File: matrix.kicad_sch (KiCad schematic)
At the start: 130 parts, among them SW1 `, SW10 9, SW11 0, SW12 -, SW13 =, SW14 BKSPC, SW15 DEL, SW16 TAB, SW17 Q, SW18 W, SW19 E, SW2 1, SW20 R, SW21 T, SW22 Y, SW23 U, SW24 I, SW25 O, SW26 P, SW27 [{, SW28 ]}, SW29 \|, SW3 2, SW30 HOME, SW31 CAPS, SW32 A, SW33 S, SW34 D, SW35 F, SW36 G, SW37 H, SW38 J, SW39 K, SW4 3, SW40 L, SW41 ;:, SW42 '", SW43 ENTER, SW44 LSHIFT, SW45 Z, SW46 X, SW47 C, SW48 V, SW49 B, SW5 4, SW50 N, SW51 M, SW52 ,<, SW53 .>, SW54 /?, SW55 RSHIFT, SW56 UP, SW57 LCTRL, SW58 LWIN, SW59 LALT, SW6 5, SW60 SPACE, SW61 RALT, SW62 FN, SW63 LEFT, SW64 DOWN, SW65 RIGHT, SW7 6, SW8 7, SW9 8

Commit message: Wiring
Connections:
- net col10: no longer SW61.1
- net col5: now also SW60.1
- net col6: no longer SW60.1
- net col9: now also SW61.1
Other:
- moved on the sheet: D60, D61, SW60, SW61
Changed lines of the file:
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@@
   (junction (at 104.14 110.49) (diameter 0) (color 0 0 0 0)
   )
+  (junction (at 165.1 133.35) (diameter 0) (color 0 0 0 0)
+  )
   (junction (at 43.18 41.91) (diameter 0) (color 0 0 0 0)
   )
@@
   (junction (at 53.34 57.15) (diameter 0) (color 0 0 0 0)
   )
+  (junction (at 175.26 102.87) (diameter 0) (color 0 0 0 0)
+  )
   (junction (at 88.9 87.63) (diameter 0) (color 0 0 0 0)
   )
-  (junction (at 180.34 133.35) (diameter 0) (color 0 0 0 0)
-  )
   (junction (at 180.34 87.63) (diameter 0) (color 0 0 0 0)
   )
@@
   (junction (at 43.18 87.63) (diameter 0) (color 0 0 0 0)
   )
+  (junction (at 114.3 102.87) (diameter 0) (color 0 0 0 0)
+  )
   (junction (at 38.1 102.87) (diameter 0) (color 0 0 0 0)
   )
@@
   (junction (at 53.34 80.01) (diameter 0) (color 0 0 0 0)
   )
-  (junction (at 190.5 102.87) (diameter 0) (color 0 0 0 0)
-  )
   (junction (at 180.34 41.91) (diameter 0) (color 0 0 0 0)
   )
@@
   (junction (at 210.82 41.91) (diameter 0) (color 0 0 0 0)
   )
+  (junction (at 104.14 133.35) (diameter 0) (color 0 0 0 0)
+  )
   (junction (at 205.74 80.01) (diameter 0) (color 0 0 0 0)
   )
@@
   (junction (at 236.22 102.87) (diameter 0) (color 0 0 0 0)
   )
-  (junction (at 119.38 133.35) (diameter 0) (color 0 0 0 0)
-  )
   (junction (at 83.82 57.15) (diameter 0) (color 0 0 0 0)
   )
@@
   (junction (at 195.58 41.91) (diameter 0) (color 0 0 0 0)
   )
-  (junction (at 129.54 102.87) (diameter 0) (color 0 0 0 0)
-  )
   (junction (at 119.38 41.91) (diameter 0) (color 0 0 0 0)
   )
@@
     (stroke (width 0) (type default) (color 0 0 0 0))
   )
+  (wire (pts (xy 165.1 133.35) (xy 195.58 133.35))
+    (stroke (width 0) (type default) (color 0 0 0 0))
+  )
   (wire (pts (xy 149.86 64.77) (xy 165.1 64.77))
     (stroke (width 0) (type default) (color 0 0 0 0))
@@
     (stroke (width 0) (type default) (color 0 0 0 0))
   )
-  (wire (pts (xy 58.42 133.35) (xy 119.38 133.35))
-    (stroke (width 0) (type default) (color 0 0 0 0))
-  )
   (wire (pts (xy 180.34 87.63) (xy 195.58 87.63))
     (stroke (width 0) (type default) (color 0 0 0 0))
@@
     (stroke (width 0) (type default) (color 0 0 0 0))
   )
-  (wire (pts (xy 190.5 102.87) (xy 190.5 125.73))
+  (wire (pts (xy 175.26 102.87) (xy 175.26 125.73))
     (stroke (width 0) (type default) (color 0 0 0 0))
   )
@@
     (stroke (width 0) (type default) (color 0 0 0 0))
   )
-  (wire (pts (xy 180.34 133.35) (xy 195.58 133.35))
-    (stroke (width 0) (type default) (color 0 0 0 0))
-  )
   (wire (pts (xy 88.9 87.63) (xy 104.14 87.63))
     (stroke (width 0) (type default) (color 0 0 0 0))
@@
     (stroke (width 0) (type default) (color 0 0 0 0))
   )
-  (wire (pts (xy 129.54 102.87) (xy 129.54 125.73))
+  (wire (pts (xy 114.3 102.87) (xy 114.3 125.73))
     (stroke (width 0) (type default) (color 0 0 0 0))
   )
@@
     (stroke (width 0) (type default) (color 0 0 0 0))
   )
+  (wire (pts (xy 104.14 133.35) (xy 165.1 133.35))
+    (stroke (width 0) (type default) (color 0 0 0 0))
+  )
   (wire (pts (xy 104.14 87.63) (xy 119.38 87.63))
     (stroke (width 0) (type default) (color 0 0 0 0))
@@
     (stroke (width 0) (type default) (color 0 0 0 0))
   )
-  (wire (pts (xy 119.38 133.35) (xy 180.34 133.35))
+  (wire (pts (xy 58.42 133.35) (xy 104.14 133.35))
     (stroke (width 0) (type default) (color 0 0 0 0))
   )
@@
     (pin "2")
   )
-  (symbol (lib_id "Device:D") (at 180.34 129.54 90) (unit 1)
-    (in_bom yes) (on_board yes) (fields_autoplaced)
-    (property "Reference" "D61" (id 0) (at 182.88 128.2699 90)
-      (effects (font (size 1.27 1.27)) (justify right))
-    )
-    (property "Value" "D" (id 1) (at 182.88 130.8099 90)
-      (effects (font (size 1.27 1.27)) (justify right))
-    )
-    (property "Footprint" "Diode_SMD:D_SOD-123" (id 2) (at 180.34 129.54 0)
-      (effects (font (size 1.27 1.27)) hide)
-    )
-    (property "Datasheet" "~" (id 3) (at 180.34 129.54 0)
+  (symbol (lib_id "Device:D") (at 165.1 129.54 90) (unit 1)
+    (in_bom yes) (on_board yes) (fields_autoplaced)
+    (property "Reference" "D61" (id 0) (at 167.64 128.2699 90)
+      (effects (font (size 1.27 1.27)) (justify right))
+    )
+    (property "Value" "D" (id 1) (at 167.64 130.8099 90)
+      (effects (font (size 1.27 1.27)) (justify right))
+    )
+    (property "Footprint" "Diode_SMD:D_SOD-123" (id 2) (at 165.1 129.54 0)
+      (effects (font (size 1.27 1.27)) hide)
+    )
+    (property "Datasheet" "~" (id 3) (at 165.1 129.54 0)
       (effects (font (size 1.27 1.27)) hide)
     )
@@
     (pin "2")
   )
-  (symbol (lib_id "Device:D") (at 119.38 129.54 90) (unit 1)
-    (in_bom yes) (on_board yes) (fields_autoplaced)
-    (property "Reference" "D60" (id 0) (at 121.92 128.2699 90)
-      (effects (font (size 1.27 1.27)) (justify right))
-    )
-    (property "Value" "D" (id 1) (at 121.92 130.8099 90)
-      (effects (font (size 1.27 1.27)) (justify right))
-    )
-    (property "Footprint" "Diode_SMD:D_SOD-123" (id 2) (at 119.38 129.54 0)
-      (effects (font (size 1.27 1.27)) hide)
-    )
-    (property "Datasheet" "~" (id 3) (at 119.38 129.54 0)
+  (symbol (lib_id "Device:D") (at 104.14 129.54 90) (unit 1)
+    (in_bom yes) (on_board yes) (fields_autoplaced)
+    (property "Reference" "D60" (id 0) (at 106.68 128.2699 90)
+      (effects (font (size 1.27 1.27)) (justify right))
+    )
+    (property "Value" "D" (id 1) (at 106.68 130.8099 90)
+      (effects (font (size 1.27 1.27)) (justify right))
+    )
+    (property "Footprint" "Diode_SMD:D_SOD-123" (id 2) (at 104.14 129.54 0)
+      (effects (font (size 1.27 1.27)) hide)
+    )
+    (property "Datasheet" "~" (id 3) (at 104.14 129.54 0)
       (effects (font (size 1.27 1.27)) hide)
     )
@@
     (pin "2")
   )
-  (symbol (lib_id "Switch:SW_Push") (at 124.46 125.73 180) (unit 1)
-    (in_bom yes) (on_board yes) (fields_autoplaced)
-    (property "Reference" "SW60" (id 0) (at 124.46 120.65 0))
-    (property "Value" "SPACE" (id 1) (at 124.46 123.19 0))
-    (property "Footprint" "MX_Only:MXOnly-6.25U" (id 2) (at 124.46 130.81 0)
-      (effects (font (size 1.27 1.27)) hide)
-    )
-    (property "Datasheet" "~" (id 3) (at 124.46 130.81 0)
+  (symbol (lib_id "Switch:SW_Push") (at 109.22 125.73 180) (unit 1)
+    (in_bom yes) (on_board yes) (fields_autoplaced)
+    (property "Reference" "SW60" (id 0) (at 109.22 120.65 0))
+    (property "Value" "SPACE" (id 1) (at 109.22 123.19 0))
+    (property "Footprint" "MX_Only:MXOnly-6.25U" (id 2) (at 109.22 130.81 0)
+      (effects (font (size 1.27 1.27)) hide)
+    )
+    (property "Datasheet" "~" (id 3) (at 109.22 130.81 0)
       (effects (font (size 1.27 1.27)) hide)
     )
@@
     (pin "2")
   )
-  (symbol (lib_id "Switch:SW_Push") (at 185.42 125.73 180) (unit 1)
-    (in_bom yes) (on_board yes) (fields_autoplaced)
-    (property "Reference" "SW61" (id 0) (at 185.42 120.65 0))
-    (property "Value" "RALT" (id 1) (at 185.42 123.19 0))
-    (property "Footprint" "MX_Only:MXOnly-1.25U" (id 2) (at 185.42 130.81 0)
-      (effects (font (size 1.27 1.27)) hide)
-    )
-    (property "Datasheet" "~" (id 3) (at 185.42 130.81 0)
-      (effects (font (size 1.27 1.27)) hide)
-    )
+  (symbol (lib_id "Switch:SW_Push") (at 170.18 125.73 180) (unit 1)
+    (in_bom yes) (on_board yes) (fields_autoplaced)
+    (property "Reference" "SW61" (id 0) (at 170.18 120.65 0))
+    (property "Value" "RALT" (id 1) (at 170.18 123.19 0))
+    (property "Footprint" "MX_Only:MXOnly-1.25U" (id 2) (at 170.18 130.81 0)
+      (effects (font (size 1.27 1.27)) hide)
+    )
+    (property "Datasheet" "~" (id 3) (at 170.18 130.81 0)
+      (effects (font (size 1.27 1.27)) hide)
+    )

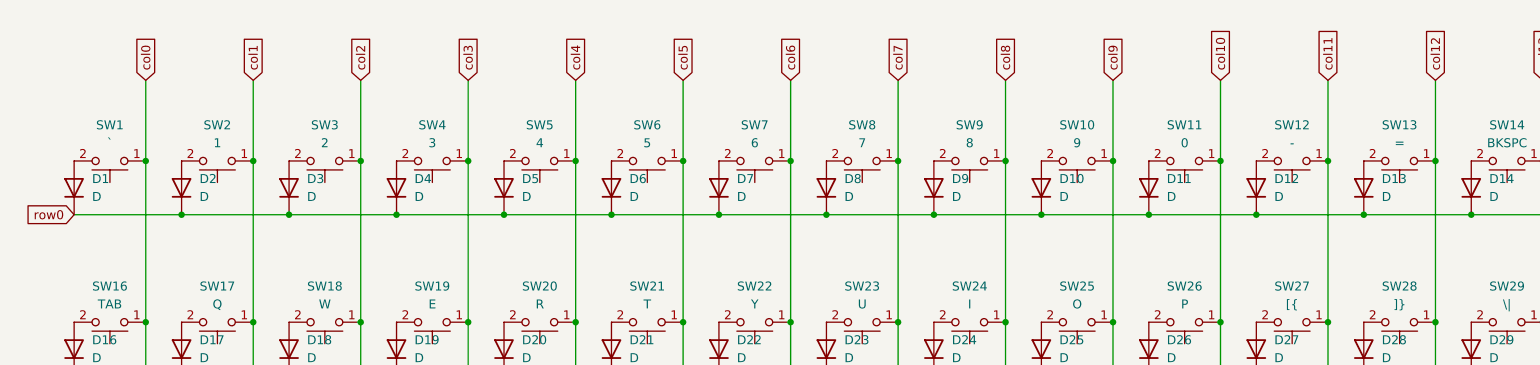
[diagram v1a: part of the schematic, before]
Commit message: Routing Complete
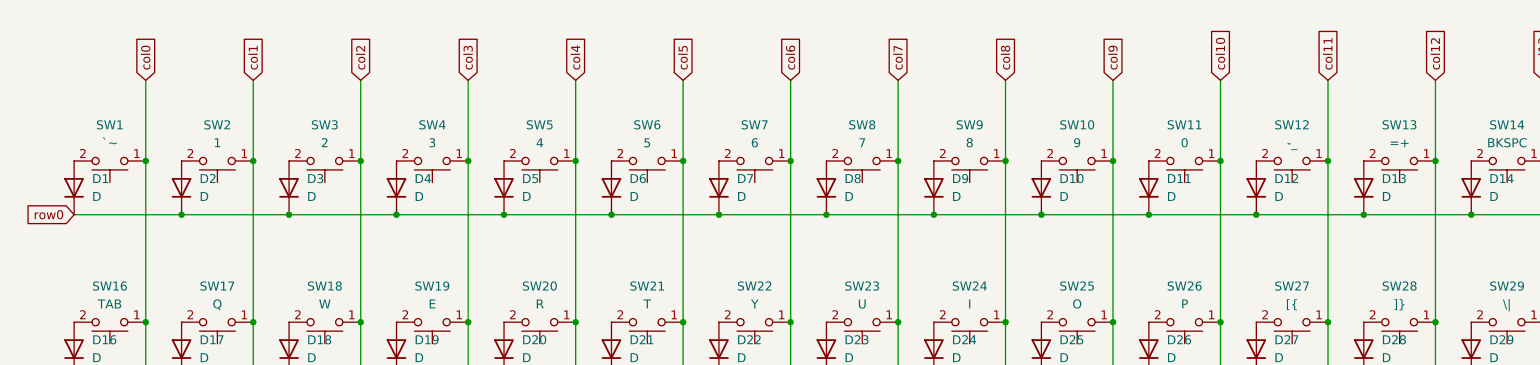
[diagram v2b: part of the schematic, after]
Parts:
- SW1: value ` -> `~
- SW12: value - -> -_
- SW13: value = -> =+
- SW60: footprint MX_Only:MXOnly-6.25U -> MX_Only:MXOnly-6.25U-ReversedStabilizers
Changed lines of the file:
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@@
     (in_bom yes) (on_board yes) (fields_autoplaced)
     (property "Reference" "SW13" (id 0) (at 215.9 29.21 0))
-    (property "Value" "=" (id 1) (at 215.9 31.75 0))
+    (property "Value" "=+" (id 1) (at 215.9 31.75 0))
     (property "Footprint" "MX_Only:MXOnly-1U" (id 2) (at 215.9 39.37 0)
       (effects (font (size 1.27 1.27)) hide)
@@
     (in_bom yes) (on_board yes) (fields_autoplaced)
     (property "Reference" "SW12" (id 0) (at 200.66 29.21 0))
-    (property "Value" "-" (id 1) (at 200.66 31.75 0))
+    (property "Value" "-_" (id 1) (at 200.66 31.75 0))
     (property "Footprint" "MX_Only:MXOnly-1U" (id 2) (at 200.66 39.37 0)
       (effects (font (size 1.27 1.27)) hide)
@@
     (in_bom yes) (on_board yes) (fields_autoplaced)
     (property "Reference" "SW1" (id 0) (at 33.02 29.21 0))
-    (property "Value" "`" (id 1) (at 33.02 31.75 0))
+    (property "Value" "`~" (id 1) (at 33.02 31.75 0))
     (property "Footprint" "MX_Only:MXOnly-1U" (id 2) (at 33.02 39.37 0)
       (effects (font (size 1.27 1.27)) hide)
@@
     (property "Reference" "SW60" (id 0) (at 109.22 120.65 0))
     (property "Value" "SPACE" (id 1) (at 109.22 123.19 0))
-    (property "Footprint" "MX_Only:MXOnly-6.25U" (id 2) (at 109.22 130.81 0)
-      (effects (font (size 1.27 1.27)) hide)
-    )
+    (property "Footprint" "MX_Only:MXOnly-6.25U-ReversedStabilizers" (id 2) (at 109.22 130.81 0)
+      (effects (font (size 1.27 1.27)) hide)
+    )
